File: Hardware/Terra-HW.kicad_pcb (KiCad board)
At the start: 4 copper layers, 76.9 x 67.3 mm, 97 parts, among them J1 GT-USB-7010ASV, J2 S2B-PH-SM4-TB, J3 0532610271, J4 Conn_Coaxial, J5 B8B-PH-SM4-TB, Q1 DMP3099L, Q2 2N7002, Q3 2N7002, SW2 KMR231NG, SW3 KMR231NG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

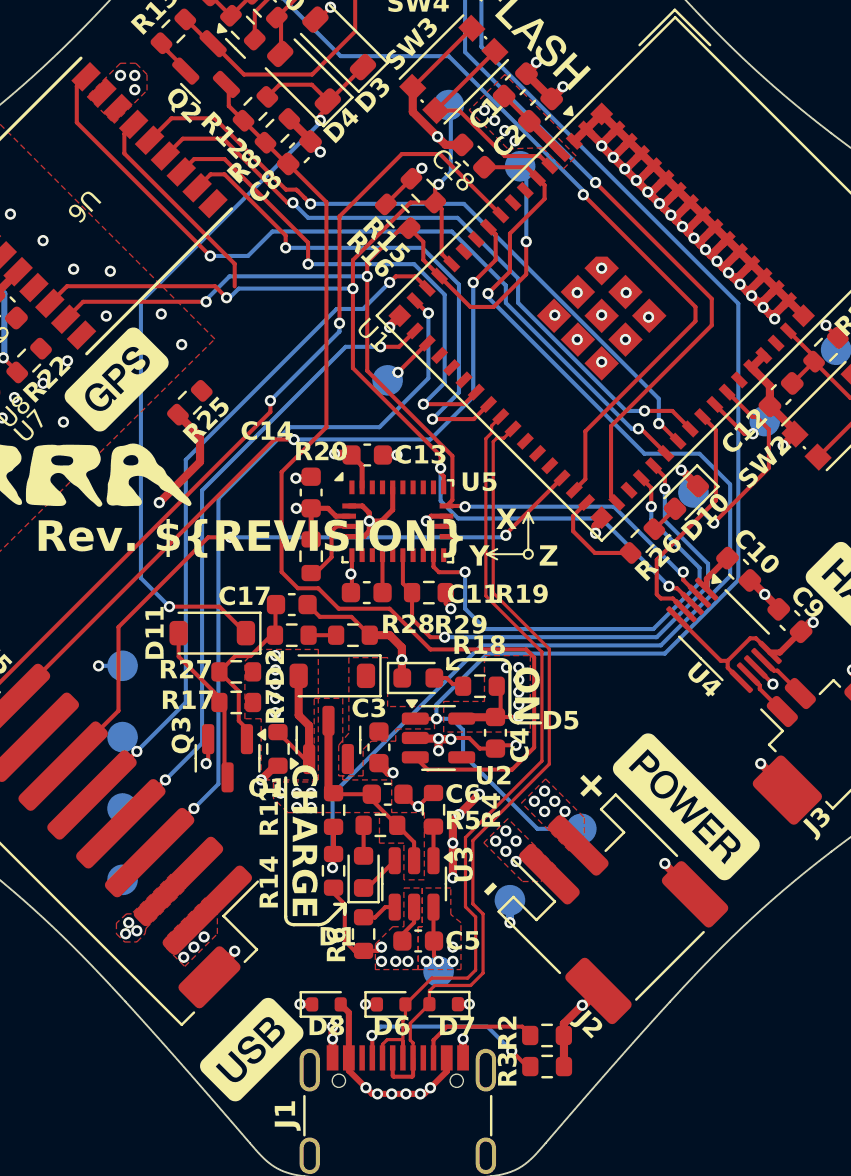
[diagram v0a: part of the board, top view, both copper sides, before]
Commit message: pcb: move power connector in from edge 1mm
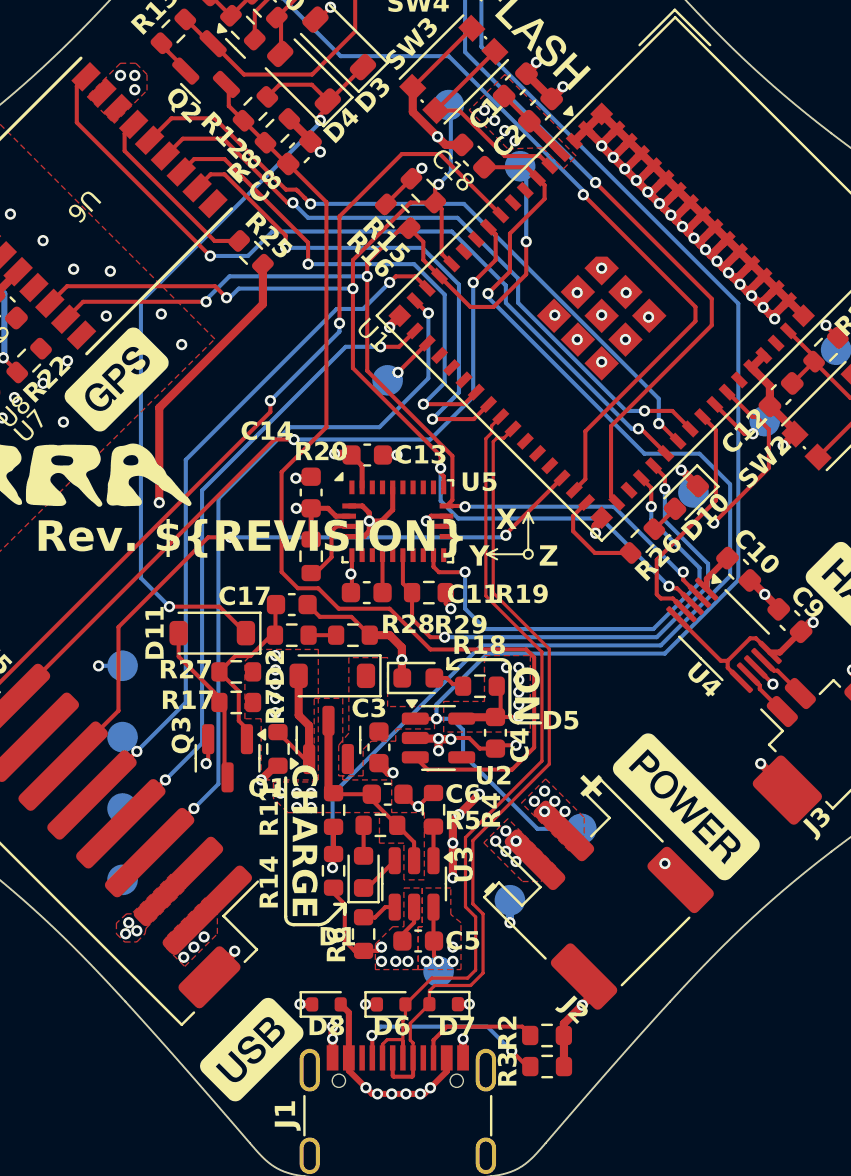
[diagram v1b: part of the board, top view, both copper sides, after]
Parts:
- moved R25 7.94 mm to (142.8, 80.3), turned to 135 degrees
- moved J2 1.00 mm to (159.5, 111.4)
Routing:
- net VBAT: track 31.6 -> 39.8 mm
- net /Peripehrals/GPS_VBAT: track 10.4 -> 8.93 mm

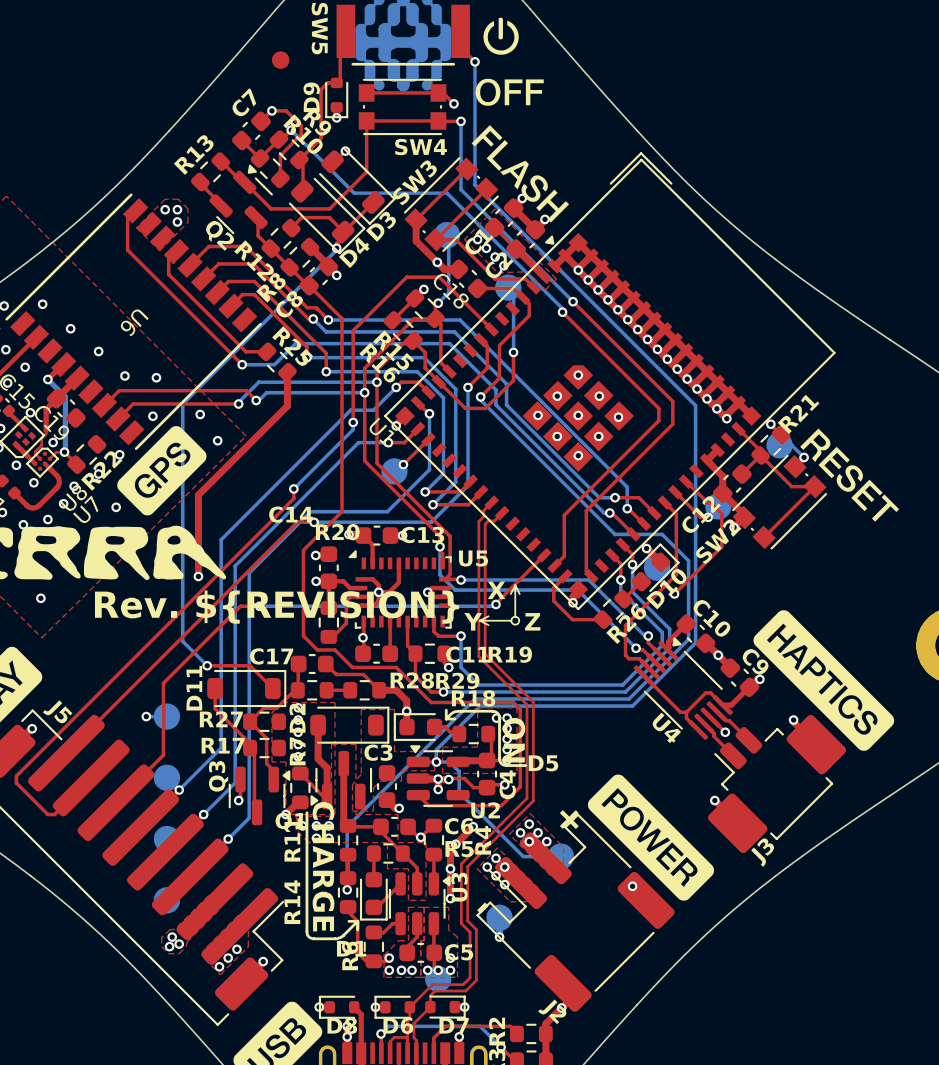
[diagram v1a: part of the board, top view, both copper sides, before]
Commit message: pcb: route new pwroff signals
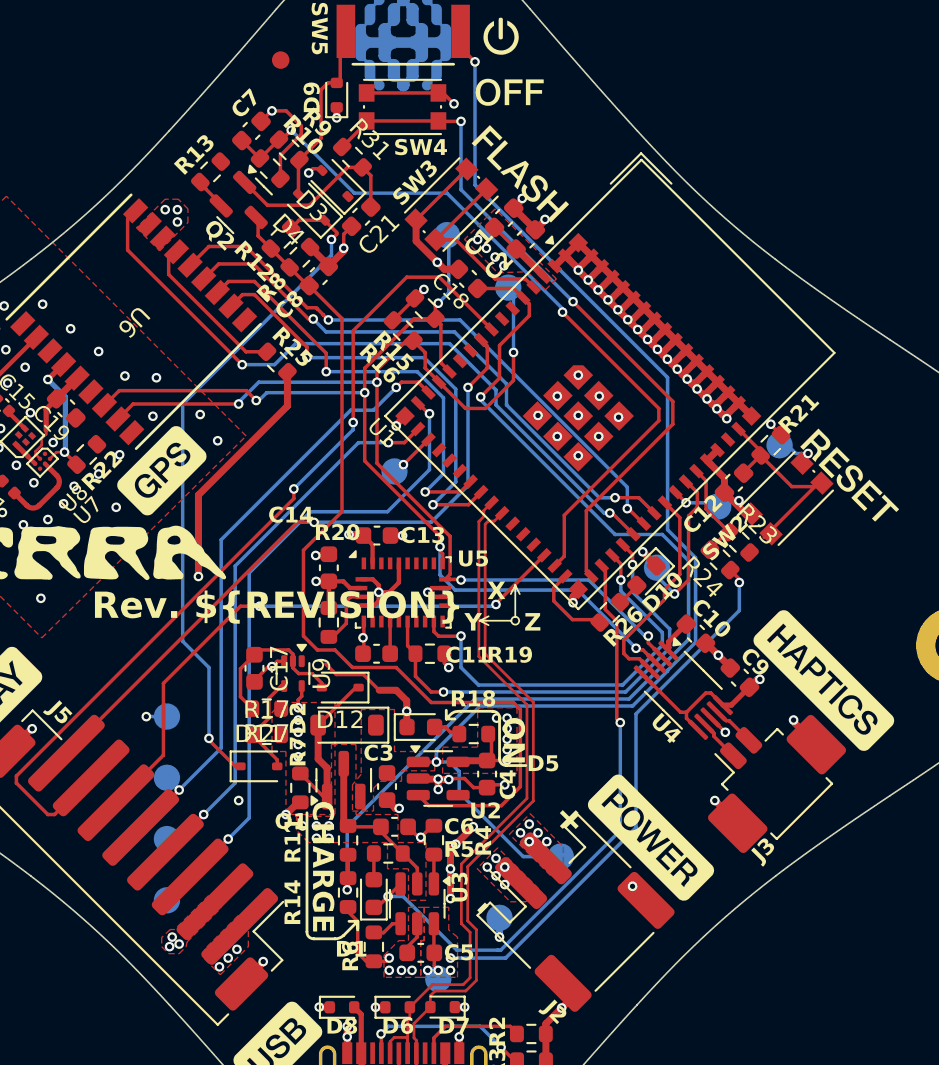
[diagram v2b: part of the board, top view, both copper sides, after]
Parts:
- removed Q3: 2N7002, Package_TO_SOT_SMD:SOT-23
- removed R28, R29: 100k, Resistor_SMD:R_0603_1608Metric
- added C21: 0.1u, Capacitor_SMD:C_0603_1608Metric, F.Cu at (147.6, 72.0)
- added D12: B5819WS-TP, Diode_SMD:D_SOD-323, F.Cu at (146.4, 98.9)
- added R23: 100k, Resistor_SMD:R_0603_1608Metric, F.Cu at (169.2, 90.6)
- added R24: 100k, Resistor_SMD:R_0603_1608Metric, F.Cu at (168.1, 91.6)
- added R31: 1.5k, Resistor_SMD:R_0603_1608Metric, F.Cu at (147.1, 68.6)
- added U9: SN74LVC1G14DRL, Package_TO_SOT_SMD:SOT-553, F.Cu at (143.7, 98.1)
- D11, D3, D4: value PMEG2010AEH -> B5819WS-TP; footprint Diode_SMD:D_SOD-123 -> Diode_SMD:D_SOD-323
- moved D11 4.53 mm to (141.8, 103.4), turned to 0 degrees
- moved C17 3.31 mm to (141.5, 97.8), turned to -90 degrees
- moved D3 1.03 mm to (146.1, 70.1)
- moved R17 0.76 mm to (142.2, 101.6)
- moved R27 0.76 mm to (142.2, 100.1)
- moved D4 0.69 mm to (144.8, 71.5)
- moved SW2 0.45 mm to (171.9, 88.1)
- moved D10 0.33 mm to (163.9, 92.5)
- moved R26 0.26 mm to (161.8, 94.6)
- moved C12 0.11 mm to (168.9, 87.2)
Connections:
- D1 pad 1: /Power/BAT_~{CHG} -> /Microcontroller/BAT_~{CHG}
- Q2 pad 1: /Microcontroller/PWROFF -> Net-(Q2-G)
- R13 pad 2: /Microcontroller/PWROFF -> Net-(Q2-G)
- U1 pad 32: unconnected-(U1-SPIIO7/GPIO36/FSPICLK/SUBSPICLK-Pad32) -> /Microcontroller/BAT_~{CHG}
- U1 pad 41: unconnected-(U1-GPIO45-Pad41) -> /Microcontroller/USB_CONN
- U3 pad 3: /Power/BAT_~{CHG} -> /Microcontroller/BAT_~{CHG}
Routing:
- net VUSB: track 19.1 -> 54.7 mm, vias 15 -> 16
- net /Microcontroller/BAT_~{CHG}: track 0.00 -> 34.9 mm, vias 0 -> 2
- net /Microcontroller/PWROFF: track 51.6 -> 40.6 mm
- net Net-(Q2-G): track 0.00 -> 10.6 mm
- net /Microcontroller/USB_CONN: track 0.00 -> 5.77 mm
- net GND: track 142.9 -> 146.1 mm, vias 123 -> 124
- net /Power/BAT_~{CHG}: track 1.89 -> 0.00 mm
- net Net-(R28-Pad2): track 1.35 -> 0.00 mm
- net /Microcontroller/U0RXD: track 9.90 -> 8.63 mm
- net Net-(D11-A): track 7.25 -> 6.04 mm
- net Net-(D12-A): track 8.00 -> 9.14 mm
- net Net-(D11-K): track 39.6 -> 38.8 mm

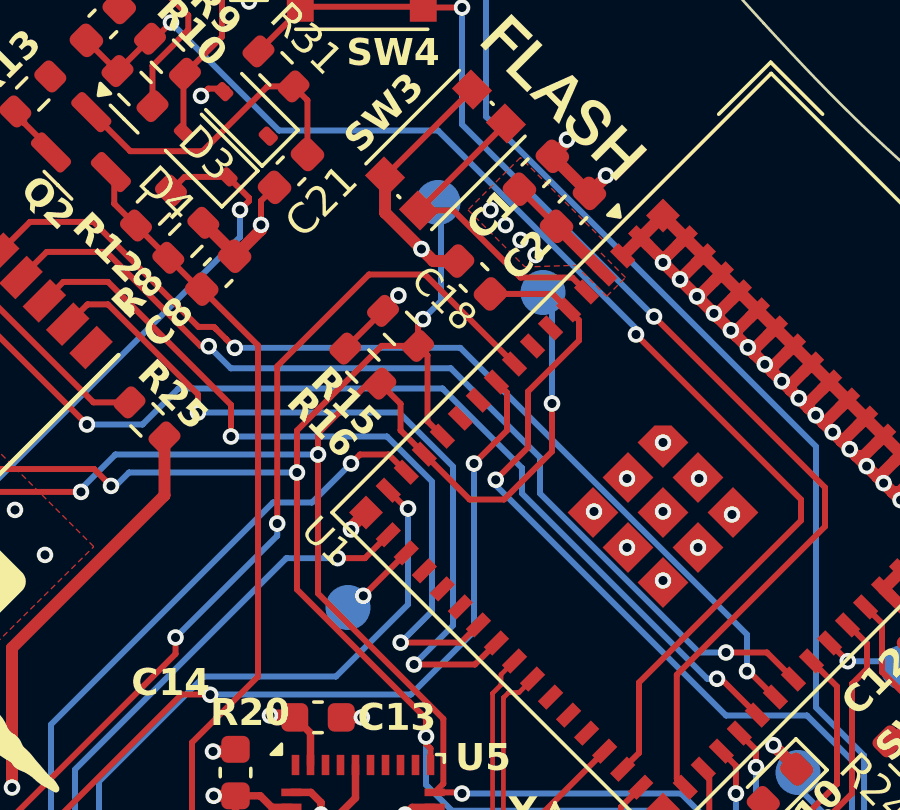
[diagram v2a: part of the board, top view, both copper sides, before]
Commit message: pcb: move back graphics and tp. remove MISO tp.
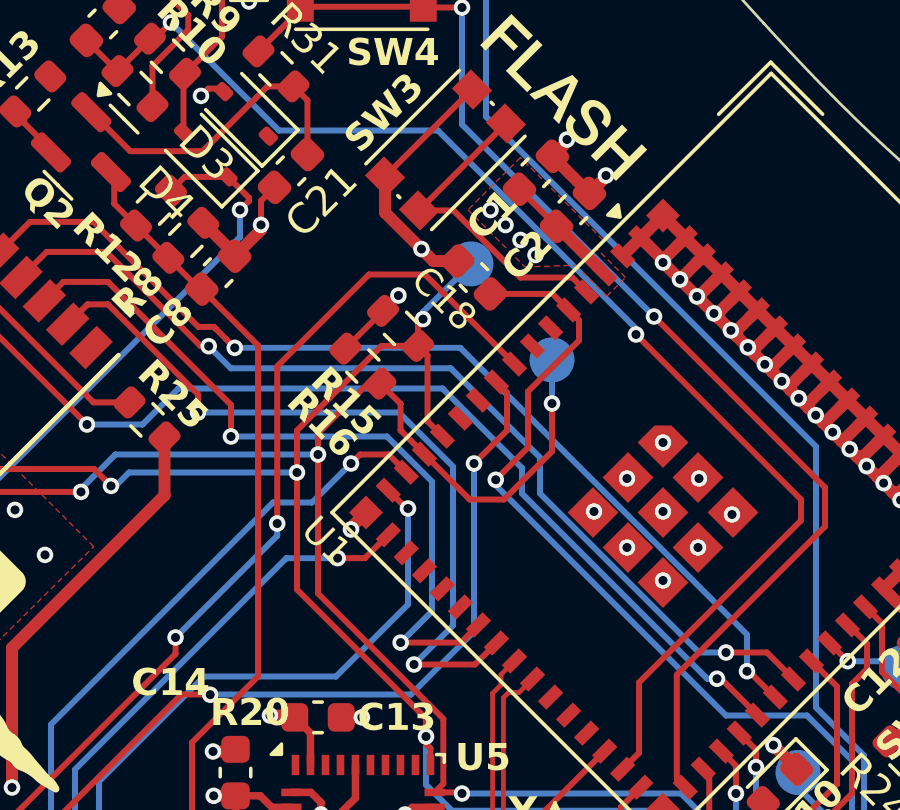
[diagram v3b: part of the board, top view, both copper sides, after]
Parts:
- removed TP12: TXD0, M20048-1:TestPoint_Pad_D1.5mm_WITH_LABEL
- moved TP7 2.32 mm to (153.6, 75.1)
- moved TP8 2.27 mm to (156.3, 78.3)
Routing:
- net /Microcontroller/SPI_MISO: track 2.03 -> 0.00 mm, vias 1 -> 0
- net /Microcontroller/I2C_SCL: track 59.9 -> 57.9 mm
- net /Microcontroller/I2C_SDA: track 58.2 -> 56.7 mm

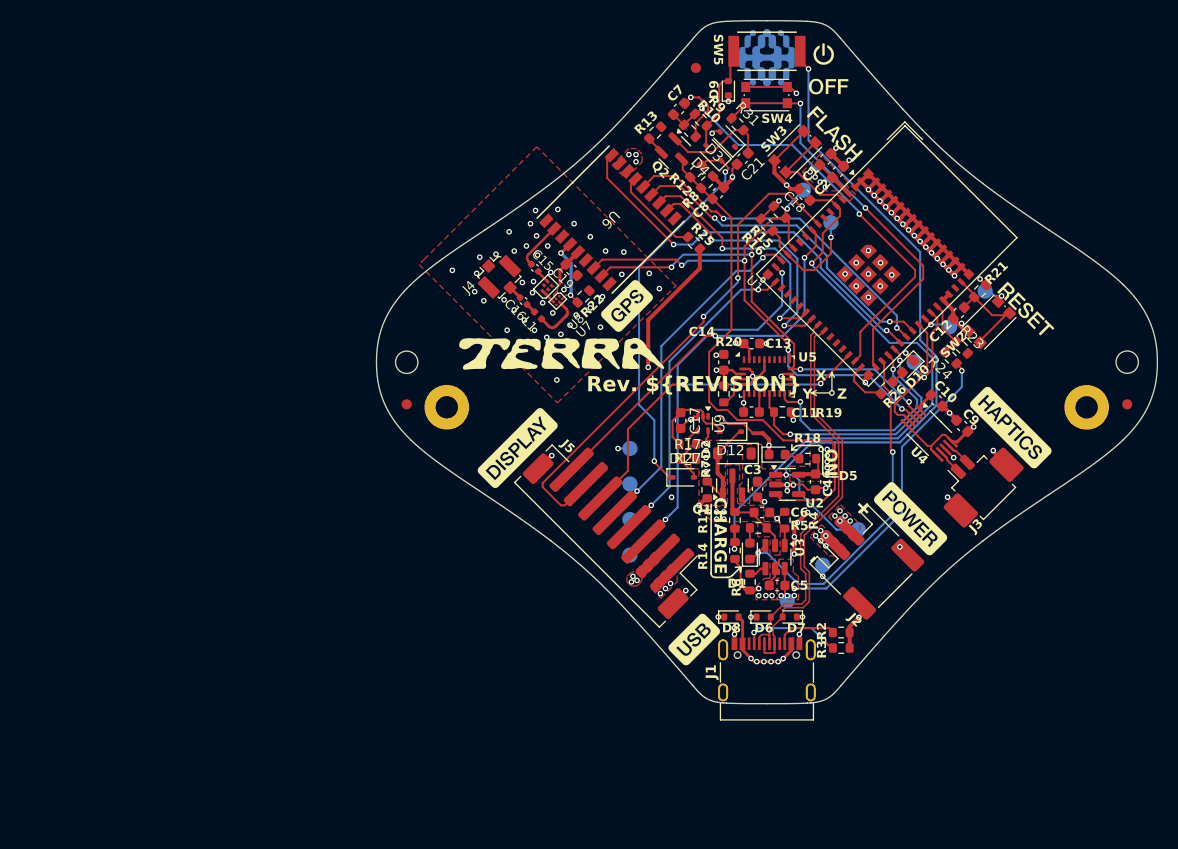
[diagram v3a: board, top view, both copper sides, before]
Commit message: pcb: position + link 3d model for gps
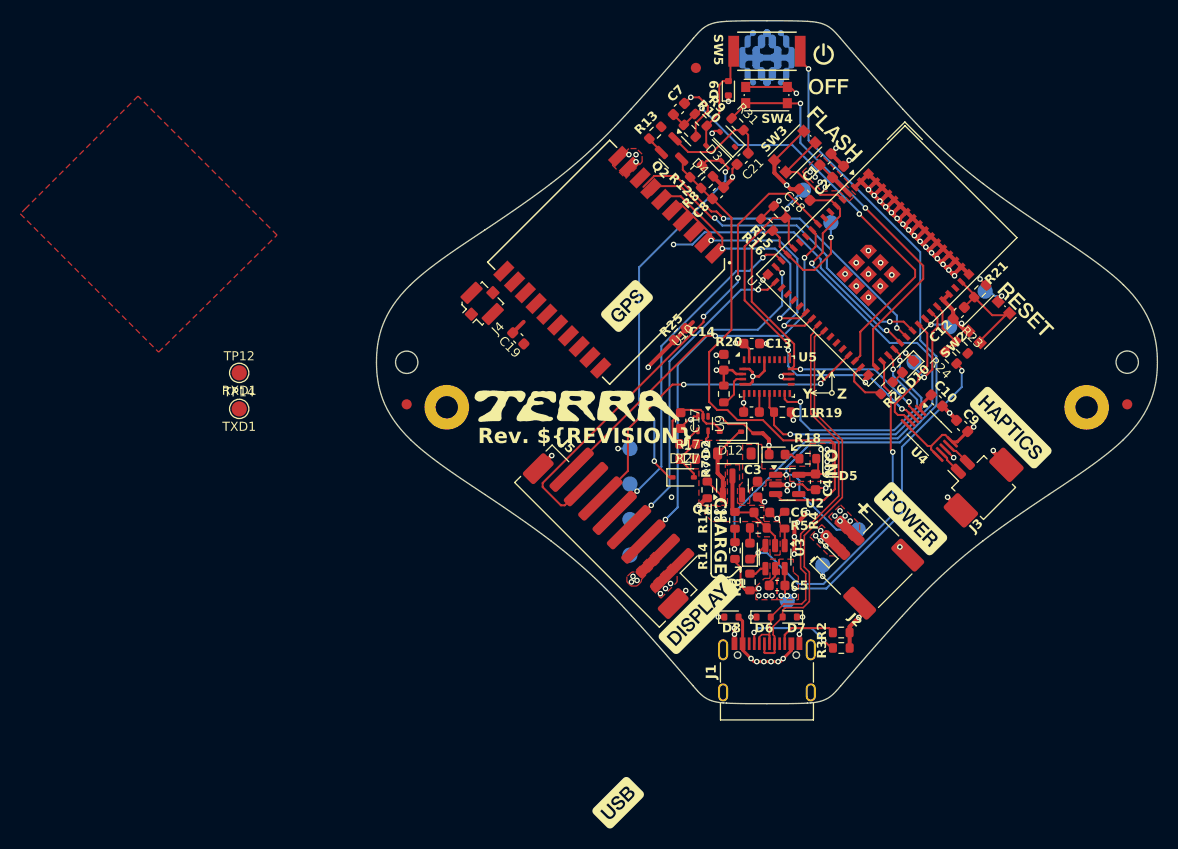
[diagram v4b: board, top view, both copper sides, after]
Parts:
- removed C15, C16: 120p, Capacitor_SMD:C_0402_1005Metric
- removed L1: 5.6n, Inductor_SMD:L_0402_1005Metric
- removed R22: 10k, Resistor_SMD:R_0603_1608Metric
- removed U6: TESEO-LIV3F, TESO-LIV3F:LCC-18_9P7X10P1_STM
- removed U7: BGA725L6, Symbols:BGA-6_2x3_0.8x1.2mm
- removed U8: B4327, Symbols:SOIC-5 B4327
- added TP12: RXD1, M20048-1:TestPoint_Pad_D1.5mm_WITH_LABEL, F.Cu at (98.0, 93.1)
- added TP14: TXD1, M20048-1:TestPoint_Pad_D1.5mm_WITH_LABEL, F.Cu at (98.0, 96.7)
- added U10: PA1616D (5186), TESO-LIV3F:PA1616D, F.Cu at (134.5, 82.2)
- R11, R14: value 10k -> 100k
- moved R25 9.09 mm to (141.5, 89.3), turned to -135 degrees
- moved C19 8.55 mm to (125.5, 89.7)
- moved J4 3.12 mm to (122.0, 86.3), turned to 135 degrees
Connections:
- C19 pad 1: +3.3V_RF -> +3.3V
- R14 pad 1: /Microcontroller/VBAT_OVER_2 -> GND
- R14 pad 2: GND -> /Microcontroller/VBAT_OVER_2
- R31 pad 1: /Microcontroller/PWROFF -> /Power/PWROFF
- SW4 pad 2: /Microcontroller/PWROFF -> /Power/PWROFF
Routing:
- net /Microcontroller/I2C_SCL: track 57.9 -> 42.2 mm, vias 5 -> 3
- net /Microcontroller/I2C_SDA: track 56.7 -> 41.1 mm, vias 5 -> 3
- net /Microcontroller/GPS_~{RST}: track 39.5 -> 27.9 mm
- net /Peripehrals/GPS_VBAT: track 8.93 -> 0.00 mm
- net /Peripehrals/ANT_EN: track 7.83 -> 0.00 mm, vias 2 -> 0
- net VBAT: track 39.8 -> 32.3 mm
- net +3.3V_RF: track 6.05 -> 0.00 mm
- net Net-(U7-A_{IN}): track 4.91 -> 0.00 mm
- net Net-(U6-RF_IN): track 4.75 -> 0.00 mm
- net Net-(U7-A_{OUT}): track 1.53 -> 0.00 mm
- net +3.3V: track 36.5 -> 37.9 mm, vias 25 -> 23
- net Net-(J4-In): track 1.40 -> 0.00 mm
- net Net-(U8-RF_{OUT}): track 1.40 -> 0.00 mm
- net Net-(C16-Pad1): track 1.10 -> 0.00 mm
- net GND: vias 124 -> 82
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
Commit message: component placement 2SEPT2025 for P&T
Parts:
- TP12, TP14: moved to B.Cu
- moved TP14 44.4 mm to (138.5, 78.4), turned to 180 degrees
- moved TP12 42.2 mm to (136.2, 75.1), turned to 180 degrees
- moved C19 32.7 mm to (153.6, 72.8), turned to 45 degrees
- moved SW3 31.2 mm to (176.0, 92.1)
- moved C7 23.4 mm to (123.3, 82.0)
- moved R13 23.1 mm to (121.2, 84.1)
- moved R9 22.3 mm to (126.5, 82.6)
- moved R10 22.2 mm to (125.5, 83.7)
- moved Q2 22.2 mm to (123.8, 85.4)
- moved C21 21.4 mm to (131.3, 85.8)
- moved R8 21.3 mm to (127.5, 87.6)
- moved R12 21.3 mm to (126.4, 86.5)
- moved D3 21.2 mm to (129.9, 83.8)
- moved D4 21.2 mm to (128.6, 85.1)
- moved R31 21.2 mm to (131.2, 82.6)
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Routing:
- net Net-(D11-K): track 38.8 -> 11.4 mm
- net /Microcontroller/U1RXD: track 26.1 -> 3.05 mm, vias 3 -> 1
- net /Microcontroller/U1TXD: track 25.2 -> 2.84 mm, vias 3 -> 1
- net /Power/PWR_EN: track 51.6 -> 30.0 mm
- net GND: track 146.1 -> 125.0 mm
- net /Microcontroller/PWROFF: track 40.6 -> 20.2 mm, vias 2 -> 1
- net /Power/PWROFF: track 0.00 -> 18.4 mm, vias 0 -> 1
- net /Microcontroller/SPI_MOSI: track 40.6 -> 55.9 mm, vias 2 -> 3
- net /Microcontroller/PWR_SW: track 42.9 -> 28.8 mm, vias 2 -> 5
- net /Microcontroller/ESP_BOOT0: track 10.8 -> 0.00 mm
- net Net-(Q2-G): track 10.6 -> 0.00 mm
- net /Microcontroller/GPS_STBY: track 33.6 -> 23.5 mm
- net /Microcontroller/HAPTIC_IN_TRG: track 12.2 -> 21.1 mm
- net /Microcontroller/GPS_FIX: track 32.7 -> 24.8 mm
- net Net-(D4-A): track 10.5 -> 3.20 mm
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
